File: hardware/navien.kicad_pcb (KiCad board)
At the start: 2 copper layers, 64.6 x 36.9 mm, 29 parts, among them J1 Conn_01x03_MountingPin, J3 S6B-XH-SM4-TB, Q1 2n7002, U1 WeMos_D1_mini, U2 THVD1406DR, U3 LM7805_TO220

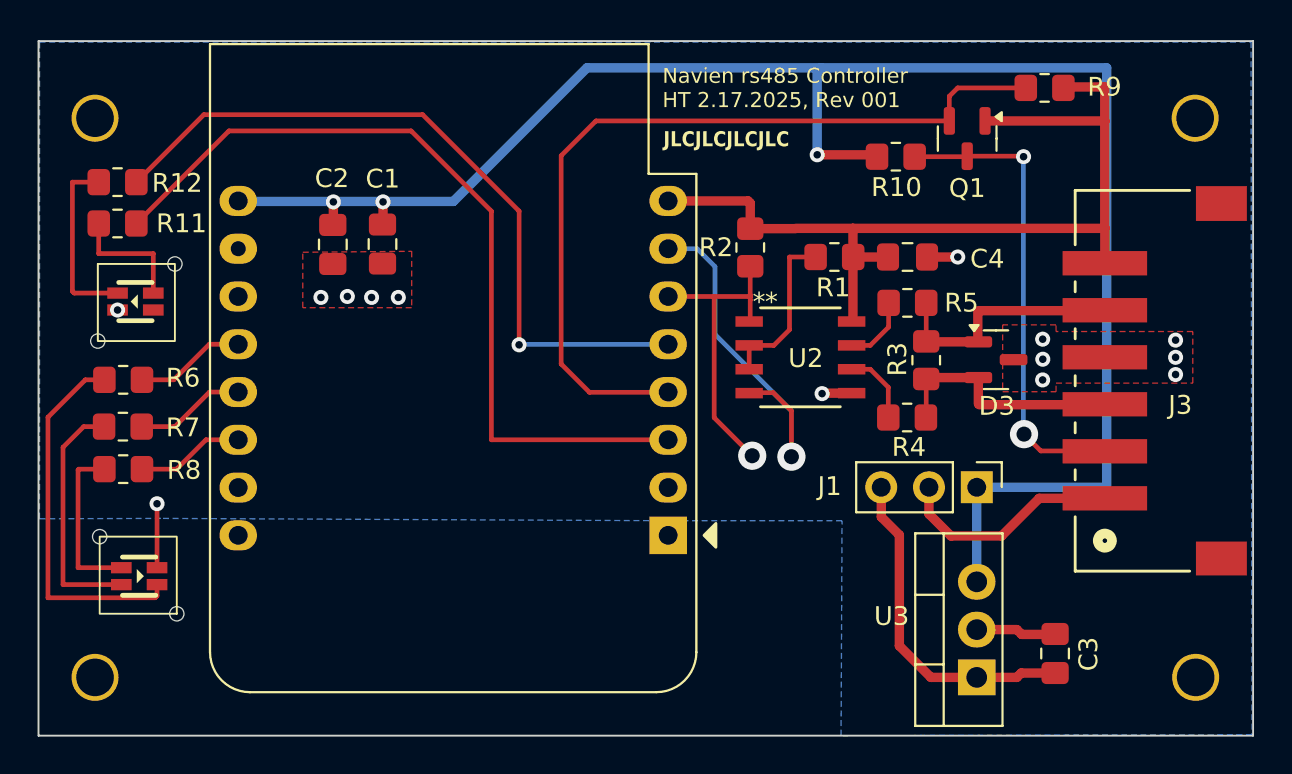
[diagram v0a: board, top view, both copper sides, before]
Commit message: Refactor(navien): extract enum-to-string helpers (op_state, heat_mode, device_type)
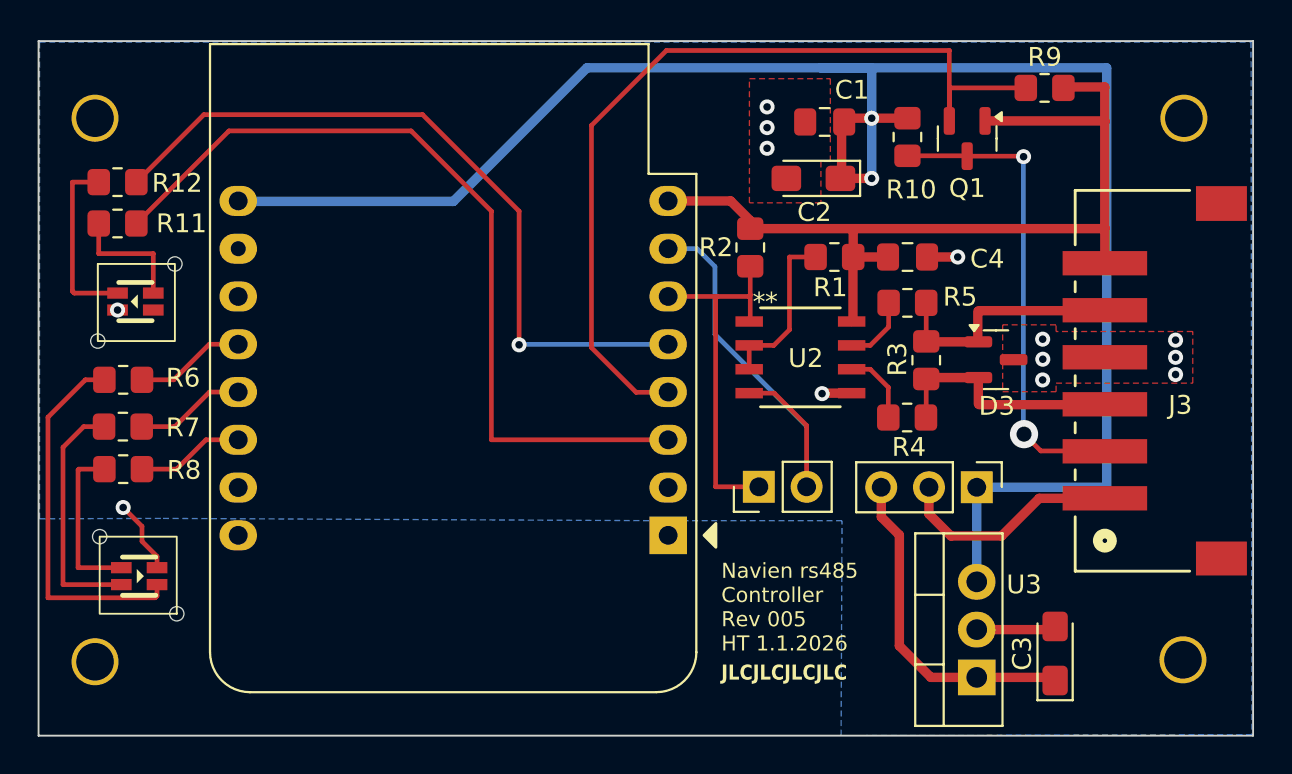
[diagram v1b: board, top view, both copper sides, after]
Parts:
- added J2: Conn_01x02, Connector_PinHeader_2.54mm:PinHeader_1x02_P2.54mm_Vertical, F.Cu at (110.6, 97.1)
- C2, C3: footprint Capacitor_SMD:C_0805_2012Metric_Pad1.18x1.45mm_HandSolder -> Capacitor_Tantalum_SMD:CP_EIA-3216-18_Kemet-A_Pad1.58x1.35mm_HandSolder
- D1: footprint LED_SMD:LED-ARRAY-SMD_4P-L1.6-W1.5-BL-FD-WITH-PIPE-2 -> BIVAR_PIPE:LED-ARRAY-SMD_4P-L1.6-W1.5-BL-FD-WITH-PIPE-2
- D5: footprint LED_SMD:LED-ARRAY-SMD_4P-L1.6-W1.5-BL-FD-WITH-PIPE-1 -> BIVAR_PIPE:LED-ARRAY-SMD_4P-L1.6-W1.5-BL-FD-WITH-PIPE-1
- R11: value 25 -> 3K
- R12: value 100 -> 3K
- R6: value 100 -> 3k
- R7: value 25 -> 3k
- R8: value 25 -> 2k
- moved C2 25.8 mm to (113.5, 80.7), turned to 180 degrees
- moved C1 24.4 mm to (114.1, 77.7), turned to 180 degrees
- moved R10 1.21 mm to (118.5, 78.5), turned to 90 degrees
- moved REF3 1.15 mm to (133.1, 106.3)
- moved REF4 0.83 mm to (75.3, 106.4)
- moved REF2 0.60 mm to (133.2, 77.5)
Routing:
- net +5V: track 94.0 -> 99.9 mm, vias 3 -> 2
- net Net-(J2-Pin_2): track 19.8 -> 23.7 mm, vias 1 -> 0
- net Net-(J2-Pin_1): track 16.7 -> 19.8 mm, vias 1 -> 0
- net Net-(Q1-S): track 44.5 -> 47.3 mm
- net Net-(U1-SDA/D2): track 6.56 -> 5.90 mm
- net GND: track 10.7 -> 11.3 mm, vias 14 -> 13
- net +3.3V: track 49.6 -> 49.1 mm
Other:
- board text added: "Navien rs485 Controller Rev 005 HT 1.1.2026"
- board text removed: "Navien rs485 Controller HT 2.17.2025, Rev 001"
